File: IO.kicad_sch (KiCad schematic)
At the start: 21 parts, among them J2 Conn_01x05_SWD, J3 Screw_Terminal_01x02_CAN, J4 Screw_Terminal_01x02_RS485, J6 Connector, USB-TYPE-C-16P, U1 SP485EEN, U4 TJA1050T/CM,118, U6 USBLC6-2SC6

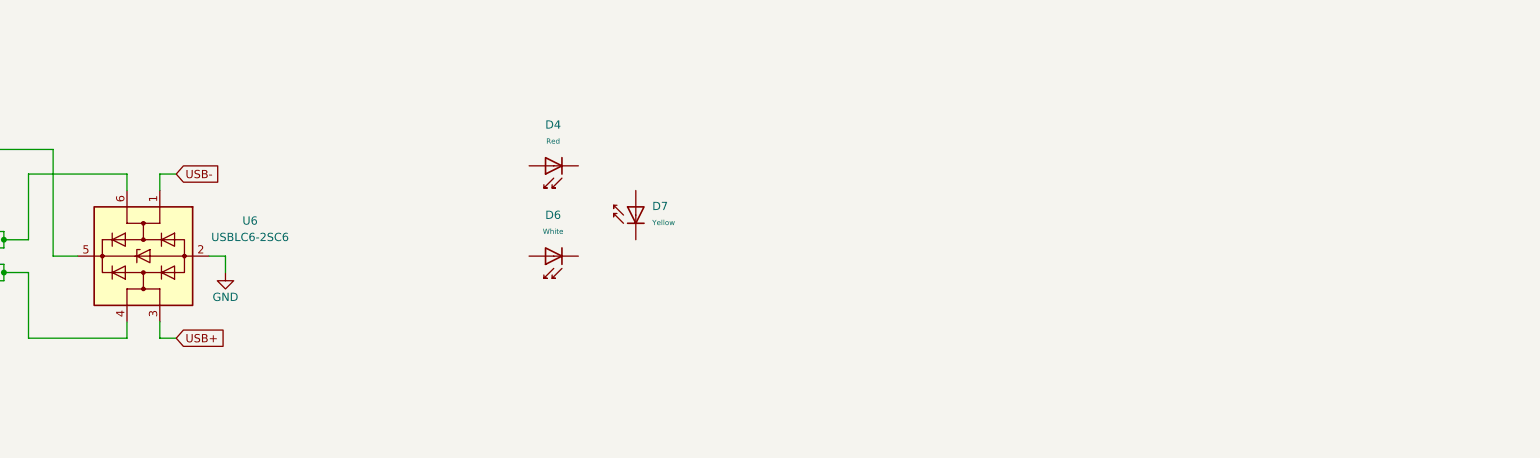
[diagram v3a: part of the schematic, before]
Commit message: Added DRV layout
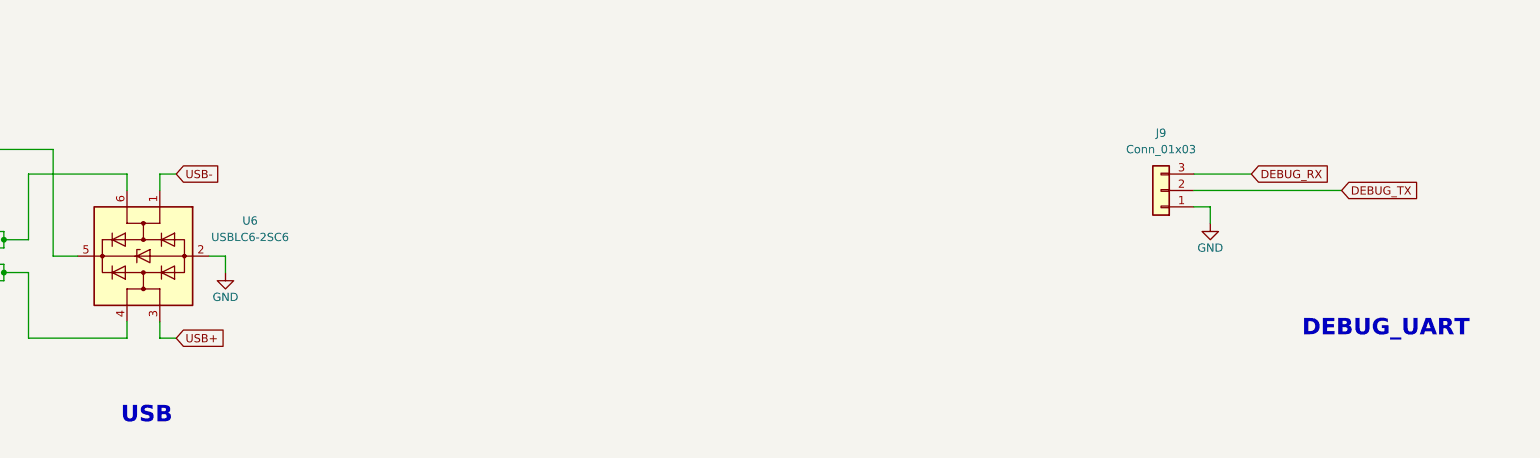
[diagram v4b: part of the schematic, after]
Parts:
- removed D4: Red, PCM_JLCPCB:D_0603, symbol PCM_JLCPCB-Diodes:LED,0603,Red
- removed D6: White, PCM_JLCPCB:D_0603, symbol PCM_JLCPCB-Diodes:LED,0603,White
- removed D7: Yellow, PCM_JLCPCB:D_0603, symbol PCM_JLCPCB-Diodes:LED,0603,Yellow
- added J9: Conn_01x03, Connector_PinHeader_2.54mm:PinHeader_1x03_P2.54mm_Vertical, symbol Connector_Generic:Conn_01x03
- J2: footprint (none) -> Connector_PinHeader_2.54mm:PinHeader_1x05_P2.54mm_Vertical
- J3, J4: footprint (none) -> Connector_Phoenix_MC:PhoenixContact_MC_1,5_2-G-3.5_1x02_P3.50mm_Horizontal
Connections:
- net GND: now also J9.1 (Pin_1)
- new net DEBUG_RX: J9.3 (Pin_3)
- new net DEBUG_TX: J9.2 (Pin_2)
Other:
- note added: "DEBUG_UART"
- note added: "USB"

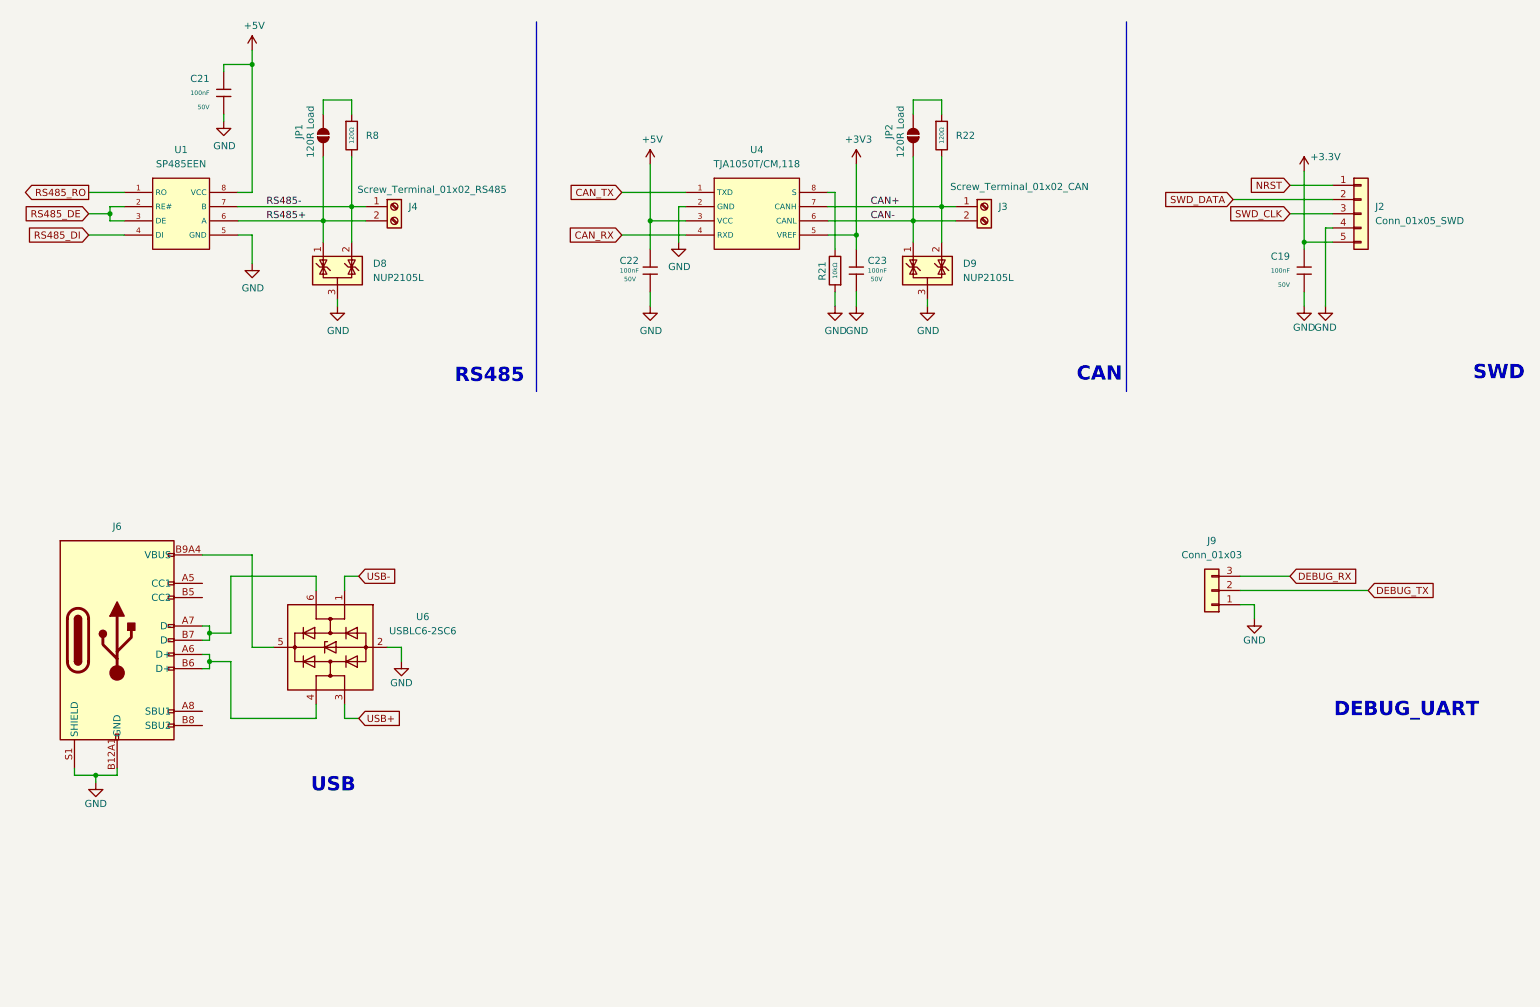
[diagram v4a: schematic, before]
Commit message: updated mcu connections
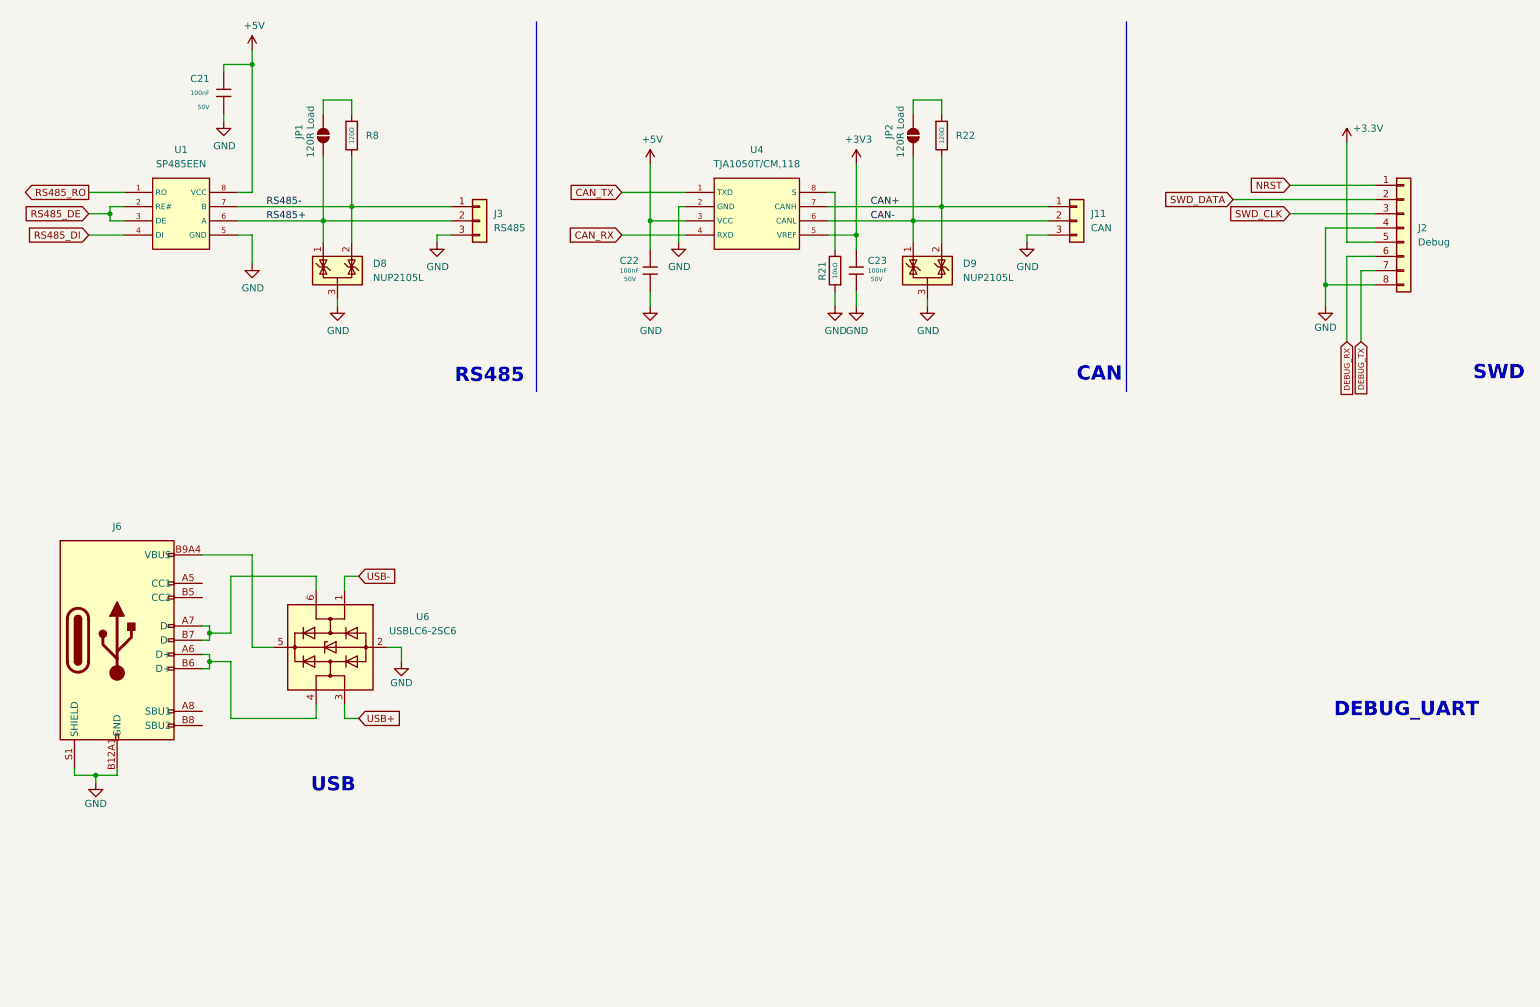
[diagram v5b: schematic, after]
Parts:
- removed C19: 100nF, PCM_JLCPCB:C_0603, symbol PCM_JLCPCB-Capacitors:0603,100nF
- removed J2: Conn_01x05_SWD, Connector_PinHeader_2.54mm:PinHeader_1x05_P2.54mm_Vertical, symbol Connector_Generic:Conn_01x05
- removed J3: Screw_Terminal_01x02_CAN, Connector_Phoenix_MC:PhoenixContact_MC_1,5_2-G-3.5_1x02_P3.50mm_Horizontal, symbol Connector:Screw_Terminal_01x02
- removed J4: Screw_Terminal_01x02_RS485, Connector_Phoenix_MC:PhoenixContact_MC_1,5_2-G-3.5_1x02_P3.50mm_Horizontal, symbol Connector:Screw_Terminal_01x02
- removed J9: Conn_01x03, Connector_PinHeader_2.54mm:PinHeader_1x03_P2.54mm_Vertical, symbol Connector_Generic:Conn_01x03
- added J11: CAN, Connector_JST:JST_GH_SM02B-GHS-TB_1x02-1MP_P1.25mm_Horizontal, symbol Connector_Generic:Conn_01x03
- added J2: Debug, Connector_JST:JST_GH_SM07B-GHS-TB_1x07-1MP_P1.25mm_Horizontal, symbol Connector_Generic:Conn_01x08
- added J3: RS485, Connector_JST:JST_GH_SM02B-GHS-TB_1x02-1MP_P1.25mm_Horizontal, symbol Connector_Generic:Conn_01x03
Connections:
- net +3.3V: now also J2.5 (Pin_5)
- net CAN+: now also J11.1 (Pin_1)
- net CAN-: now also J11.2 (Pin_2)
- net DEBUG_RX: now also J2.6 (Pin_6)
- net DEBUG_TX: now also J2.7 (Pin_7)
- net GND: now also J11.3 (Pin_3), J2.4 (Pin_4), J2.8 (Pin_8), J3.3 (Pin_3)
- net NRST: now also J2.1 (Pin_1)
- net RS485+: now also J3.2 (Pin_2)
- net RS485-: now also J3.1 (Pin_1)
- net SWD_CLK: now also J2.3 (Pin_3)
- net SWD_DATA: now also J2.2 (Pin_2)

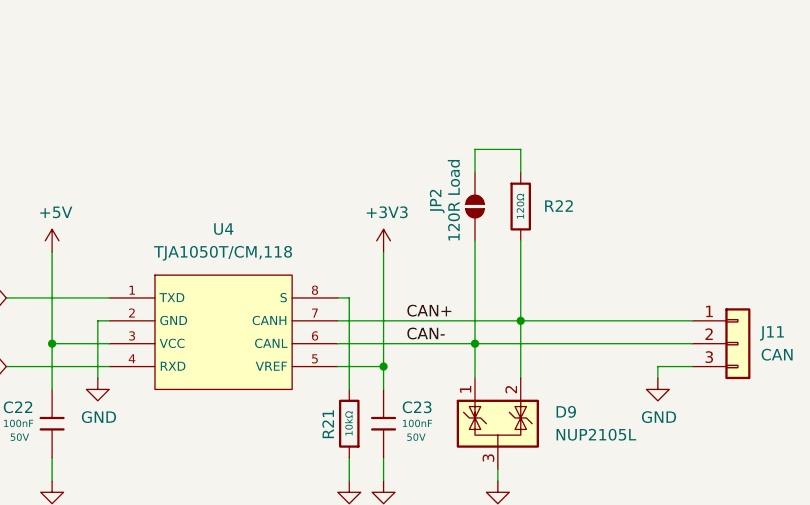
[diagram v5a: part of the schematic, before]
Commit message: Reroute mcu lines, updated can, motor timer pins
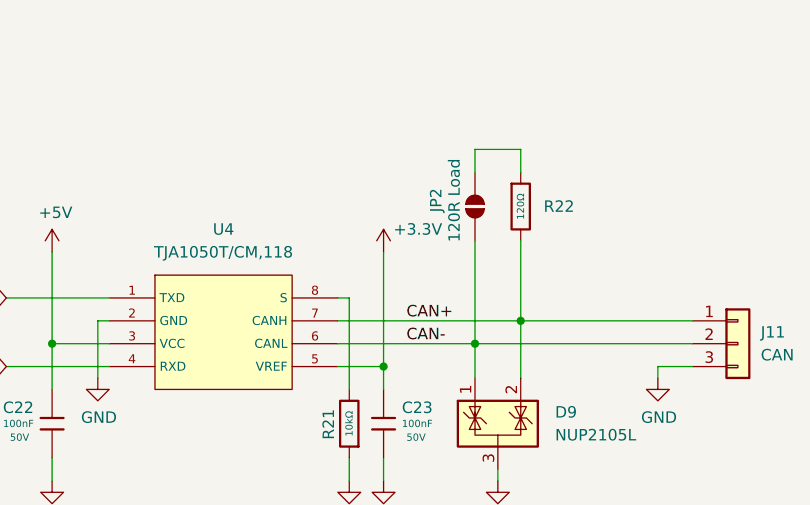
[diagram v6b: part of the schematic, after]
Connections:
- net +3V3 is gone; now on net +3.3V: C23.1, U4.5 (VREF)
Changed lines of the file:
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@@
-	)
-	(symbol
-		(lib_id "allDrive-rescue:+3.3V-power")
-		(at 165.1 41.91 0)
-		(unit 1)
-		(exclude_from_sim no)
-		(in_bom yes)
-		(on_board yes)
-		(dnp no)
-		(property "Reference" "#PWR026"
-			(at 165.1 45.72 0)
-			(effects
-				(font
-					(size 1.27 1.27)
-				)
-				(hide yes)
-			)
-		)
-		(property "Value" "+3V3"
-			(at 165.481 37.5158 0)
-			(effects
-				(font
-					(size 1.27 1.27)
-				)
-			)
-		)
-		(property "Footprint" ""
-			(at 165.1 41.91 0)
-			(effects
-				(font
-					(size 1.27 1.27)
-				)
-				(hide yes)
-			)
-		)
-		(property "Datasheet" ""
-			(at 165.1 41.91 0)
-			(effects
-				(font
-					(size 1.27 1.27)
-				)
-				(hide yes)
-			)
-		)
-		(property "Description" ""
-			(at 165.1 41.91 0)
-			(effects
-				(font
-					(size 1.27 1.27)
-				)
-			)
-		)
-		(pin "1"
-		)
-		(instances
-			(project "PiccoloMotorDriver"
-				(path "/cc8a13e7-b1a6-4cbd-adcd-4feb8b2e2369/054c4a57-633d-4e81-8316-0770c640503f"
-					(reference "#PWR026")
-					(unit 1)
-				)
-			)
-		)
 	)
 	(symbol
@@
 					(unit 1)
 				)
+			)
+		)
+	)
+	(symbol
+		(lib_id "power:+3.3V")
+		(at 165.1 41.91 0)
+		(unit 1)
+		(exclude_from_sim no)
+		(in_bom yes)
+		(on_board yes)
+		(dnp no)
+		(property "Reference" "#PWR021"
+			(at 165.1 45.72 0)
+			(effects
+				(font
+					(size 1.27 1.27)
+				)
+				(hide yes)
+			)
+		)
+		(property "Value" "+3.3V"
+			(at 168.91 39.37 0)
+			(effects
+				(font
+					(size 1.27 1.27)
+				)
+			)
+		)
+		(property "Footprint" ""
+			(at 165.1 41.91 0)
+			(effects
+				(font
+					(size 1.27 1.27)
+				)
+				(hide yes)
+			)
+		)
+		(property "Datasheet" ""
+			(at 165.1 41.91 0)
+			(effects
+				(font
+					(size 1.27 1.27)
+				)
+				(hide yes)
+			)
+		)
+		(property "Description" ""
+			(at 165.1 41.91 0)
+			(effects
+				(font
+					(size 1.27 1.27)
+				)
+			)
+		)
+		(pin "1"
+		)
+		(instances
+			(project "PiccoloMotorDriver"
+				(path "/cc8a13e7-b1a6-4cbd-adcd-4feb8b2e2369/054c4a57-633d-4e81-8316-0770c640503f"
+					(reference "#PWR021")
+					(unit 1)
+				)
